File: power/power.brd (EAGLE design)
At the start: 33.5 x 33.5 mm, 21 parts, among them IC2 FT232RL

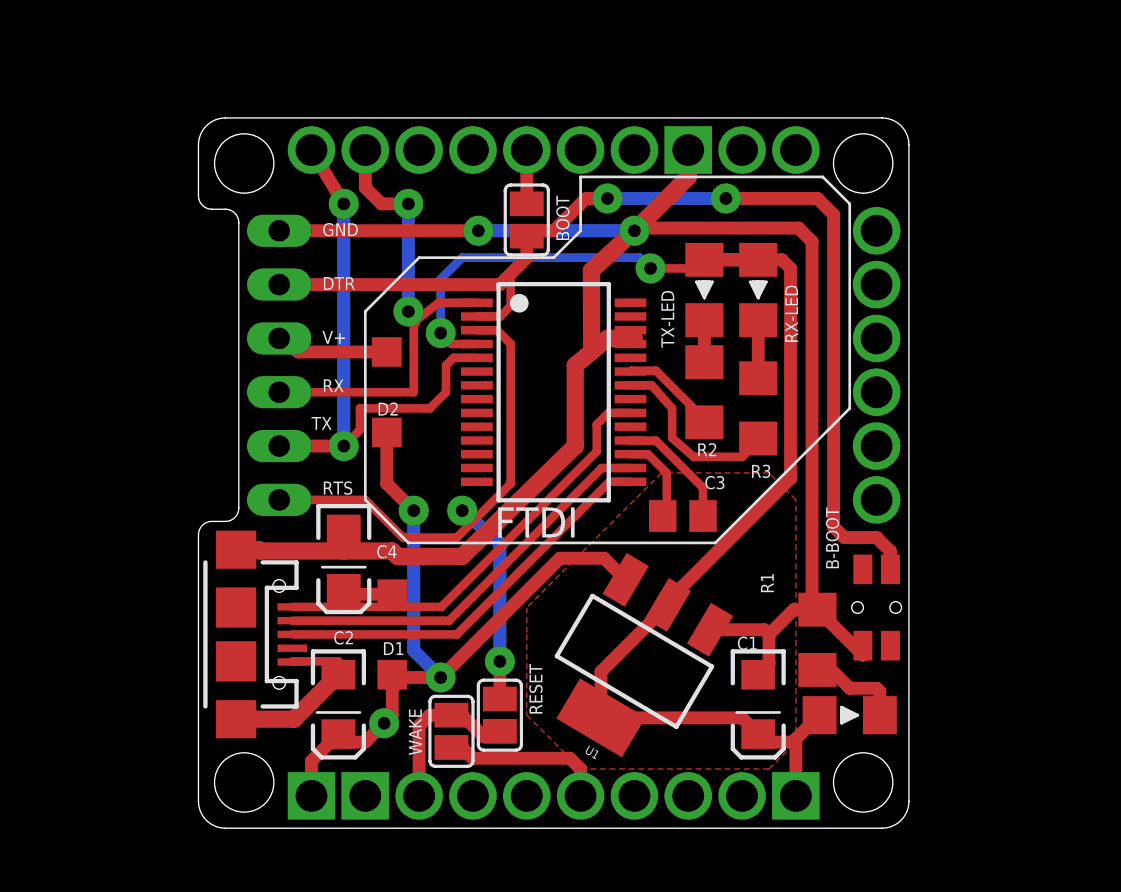
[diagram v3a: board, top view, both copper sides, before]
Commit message: Unify all boards, buttons in the same place, board dimension reduced to 1.32inch
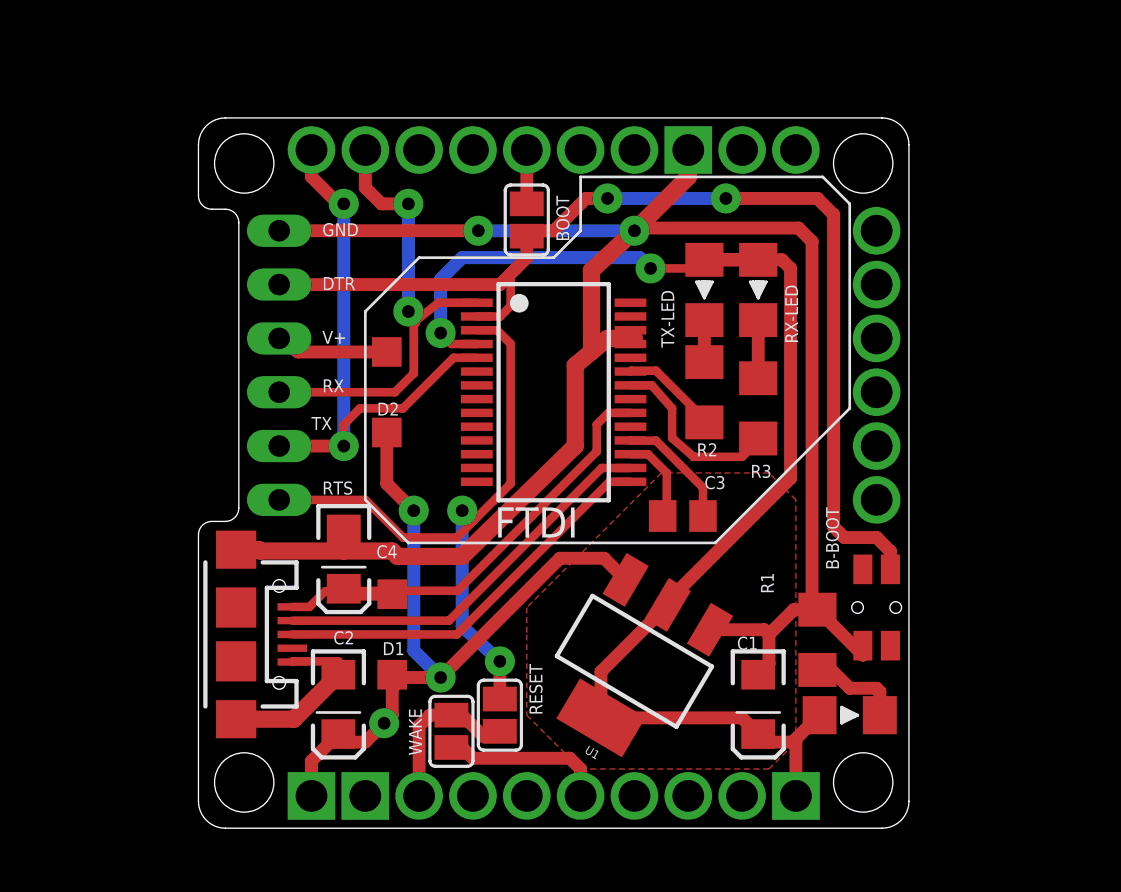
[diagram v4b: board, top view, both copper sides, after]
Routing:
- net TXD: track 22.8 -> 22.2 mm
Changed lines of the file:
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@@
 <setting verticaltext="up"/>
 </settings>
-<grid distance="0.01" unitdist="inch" unit="inch" style="lines" multiple="1" display="yes" altdistance="0.005" altunitdist="inch" altunit="inch"/>
+<grid distance="0.05" unitdist="inch" unit="inch" style="lines" multiple="1" display="no" altdistance="0.005" altunitdist="inch" altunit="inch"/>
 <layers>
 <layer number="1" name="Top" color="4" fill="1" visible="yes" active="yes"/>
@@
 <wire x1="12.965" y1="23.865" x2="12.446" y2="24.384" width="0.4064" layer="1"/>
 <via x="12.446" y="24.384" extent="1-16" drill="0.6" diameter="1.4224"/>
-<wire x1="12.446" y1="24.384" x2="12.446" y2="26.924" width="0.4064" layer="16"/>
-<wire x1="12.446" y1="26.924" x2="13.462" y2="27.94" width="0.4064" layer="16"/>
-<wire x1="13.462" y1="27.94" x2="21.844" y2="27.94" width="0.4064" layer="16"/>
-<wire x1="21.844" y1="27.94" x2="22.352" y2="27.432" width="0.4064" layer="16"/>
+<wire x1="12.446" y1="24.384" x2="12.446" y2="26.924" width="0.6096" layer="16"/>
+<wire x1="12.446" y1="26.924" x2="13.462" y2="27.94" width="0.6096" layer="16"/>
+<wire x1="13.462" y1="27.94" x2="21.844" y2="27.94" width="0.6096" layer="16"/>
+<wire x1="21.844" y1="27.94" x2="22.352" y2="27.432" width="0.6096" layer="16"/>
 <via x="22.352" y="27.432" extent="1-16" drill="0.6" diameter="1.4224"/>
 <wire x1="22.352" y1="27.432" x2="24.486" y2="27.432" width="0.4064" layer="1"/>
@@
 <vertex x="16.51" y="11.43"/>
 </polygon>
-<wire x1="23.167415625" y1="11.557265625" x2="22.86" y2="11.43" width="0" layer="19" extent="1-1"/>
 </signal>
 <signal name="GND">
@@
 <wire x1="7.874" y1="12.316" x2="7.876" y2="12.06" width="0.6096" layer="1"/>
 <wire x1="7.876" y1="12.06" x2="10.16" y2="12.06" width="0.6096" layer="1"/>
-<wire x1="12.476" y1="11.46" x2="19.812" y2="18.796" width="0.4064" layer="1"/>
+<wire x1="13.238" y1="12.222" x2="19.812" y2="18.796" width="0.4064" layer="1"/>
 <wire x1="19.812" y1="18.796" x2="19.812" y2="20.066" width="0.4064" layer="1"/>
 <wire x1="21.405" y1="20.615" x2="20.361" y2="20.615" width="0.4064" layer="1"/>
 <wire x1="20.361" y1="20.615" x2="19.812" y2="20.066" width="0.4064" layer="1"/>
-<wire x1="5.444" y1="11.46" x2="10.16" y2="11.46" width="0.4064" layer="1"/>
-<wire x1="10.16" y1="11.46" x2="12.476" y2="11.46" width="0.4064" layer="1"/>
-<wire x1="10.16" y1="12.06" x2="10.16" y2="11.46" width="0.4064" layer="1"/>
-<wire x1="12.476" y1="11.46" x2="12.446" y2="11.43" width="0" layer="19" extent="1-16"/>
+<wire x1="5.444" y1="11.46" x2="6.253" y2="11.46" width="0.4064" layer="1"/>
+<wire x1="6.253" y1="11.46" x2="6.985" y2="12.192" width="0.4064" layer="1"/>
+<wire x1="6.985" y1="12.192" x2="10.287" y2="12.222" width="0.4064" layer="1"/>
+<wire x1="10.287" y1="12.222" x2="13.238" y2="12.222" width="0.4064" layer="1"/>
+<wire x1="10.16" y1="12.06" x2="10.287" y2="12.222" width="0.4064" layer="1"/>
+<wire x1="13.238" y1="12.222" x2="12.446" y2="11.43" width="0" layer="19" extent="1-16"/>
 </signal>
 <signal name="N$2">
@@
 <wire x1="15.24" y1="7.112" x2="15.24" y2="8.89" width="0.6096" layer="1"/>
 <via x="15.24" y="8.89" extent="1-16" drill="0.6" diameter="1.4224"/>
-<wire x1="15.24" y1="8.89" x2="15.24" y2="14.478" width="0.6096" layer="16"/>
-<wire x1="15.24" y1="14.478" x2="13.462" y2="16.002" width="0.6096" layer="16"/>
+<wire x1="15.24" y1="8.89" x2="13.462" y2="10.541" width="0.6096" layer="16"/>
+<wire x1="13.462" y1="10.541" x2="13.462" y2="16.002" width="0.6096" layer="16"/>
 <via x="13.462" y="16.002" extent="1-16" drill="0.6" diameter="1.4224"/>
 <wire x1="13.462" y1="16.002" x2="13.97" y2="15.494" width="0.4064" layer="1"/>
@@
 <contactref element="POWER/FTDI" pad="RXD0"/>
 <contactref element="JP3" pad="3"/>
-<wire x1="4.826" y1="21.59" x2="11.176" y2="21.59" width="0.4064" layer="1"/>
+<wire x1="4.826" y1="21.59" x2="10.287" y2="21.59" width="0.4064" layer="1"/>
 <wire x1="14.155" y1="25.815" x2="12.353" y2="25.815" width="0.4064" layer="1"/>
 <wire x1="12.353" y1="25.815" x2="11.176" y2="24.892" width="0.4064" layer="1"/>
-<wire x1="11.176" y1="24.892" x2="11.176" y2="21.59" width="0.4064" layer="1"/>
+<wire x1="11.176" y1="24.892" x2="11.176" y2="22.479" width="0.4064" layer="1"/>
+<wire x1="11.176" y1="22.479" x2="10.287" y2="21.59" width="0.4064" layer="1"/>
 <wire x1="8.89" y1="33.02" x2="8.89" y2="31.242" width="0.6096" layer="1"/>
 <wire x1="8.89" y1="31.242" x2="9.652" y2="30.48" width="0.6096" layer="1"/>
@@
 <contactref element="JP3" pad="2"/>
 <wire x1="14.155" y1="23.215" x2="13.055" y2="23.215" width="0.4064" layer="1"/>
-<wire x1="13.055" y1="23.215" x2="12.7" y2="22.86" width="0.4064" layer="1"/>
-<wire x1="12.7" y1="22.86" x2="12.7" y2="21.59" width="0.4064" layer="1"/>
-<wire x1="12.7" y1="21.59" x2="11.938" y2="20.828" width="0.4064" layer="1"/>
-<wire x1="11.938" y1="20.828" x2="8.636" y2="20.828" width="0.4064" layer="1"/>
-<wire x1="8.636" y1="20.828" x2="8.636" y2="19.812" width="0.4064" layer="1"/>
-<wire x1="8.636" y1="19.812" x2="7.874" y2="19.05" width="0.4064" layer="1"/>
-<wire x1="6.35" y1="33.02" x2="7.874" y2="30.48" width="0.6096" layer="1"/>
+<wire x1="13.055" y1="23.215" x2="10.668" y2="20.828" width="0.4064" layer="1"/>
+<wire x1="10.668" y1="20.828" x2="8.636" y2="20.828" width="0.4064" layer="1"/>
+<wire x1="8.636" y1="20.828" x2="7.874" y2="20.066" width="0.4064" layer="1"/>
+<wire x1="7.874" y1="20.066" x2="7.874" y2="19.05" width="0.4064" layer="1"/>
+<wire x1="6.35" y1="33.02" x2="6.35" y2="31.75" width="0.6096" layer="1"/>
+<wire x1="6.35" y1="31.75" x2="7.62" y2="30.48" width="0.6096" layer="1"/>
+<wire x1="7.62" y1="30.48" x2="7.874" y2="30.48" width="0.6096" layer="1"/>
 <via x="7.874" y="30.48" extent="1-16" drill="0.6" diameter="1.4224"/>
 <wire x1="7.874" y1="30.48" x2="7.874" y2="19.05" width="0.6096" layer="16"/>
